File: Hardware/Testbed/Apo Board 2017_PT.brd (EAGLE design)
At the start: 96.5 x 62.2 mm, 18 parts

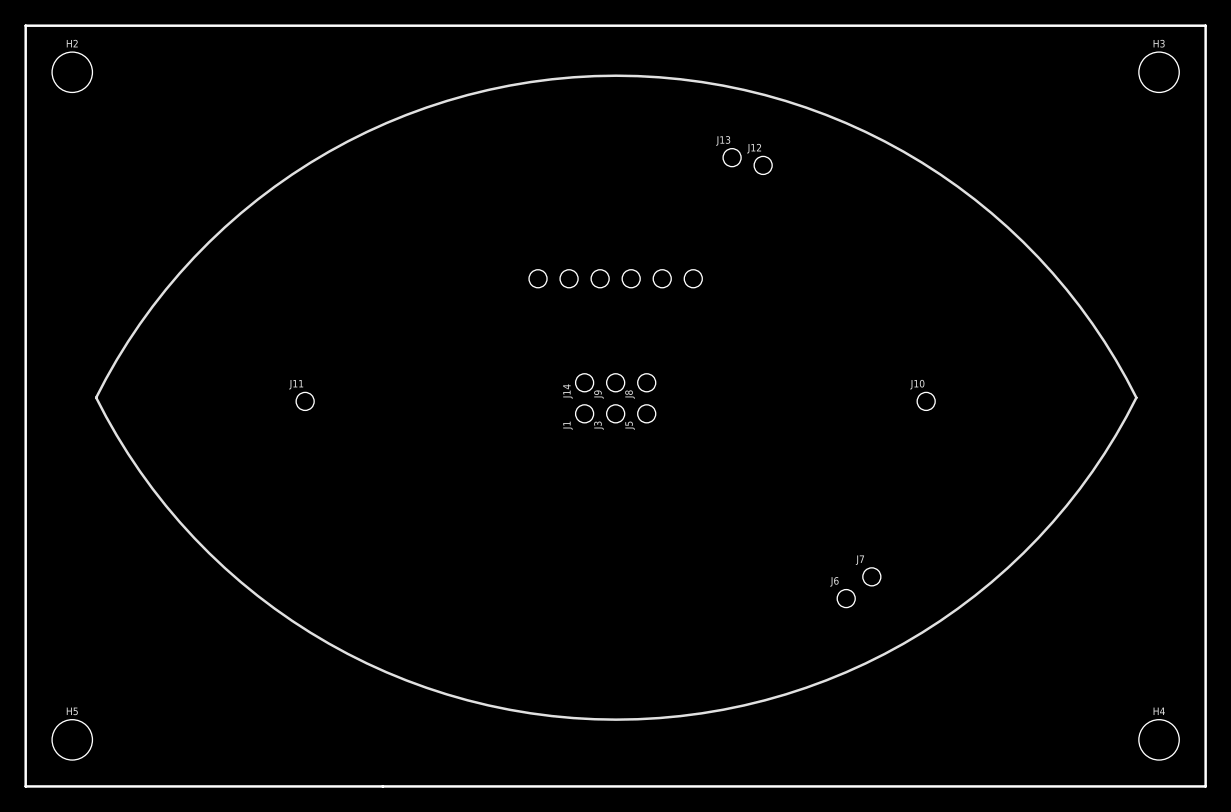
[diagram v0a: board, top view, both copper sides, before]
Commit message: Pogo Bed finished.
Finished making pogoed programming and testing fixture. Moving to
Hardware Folder
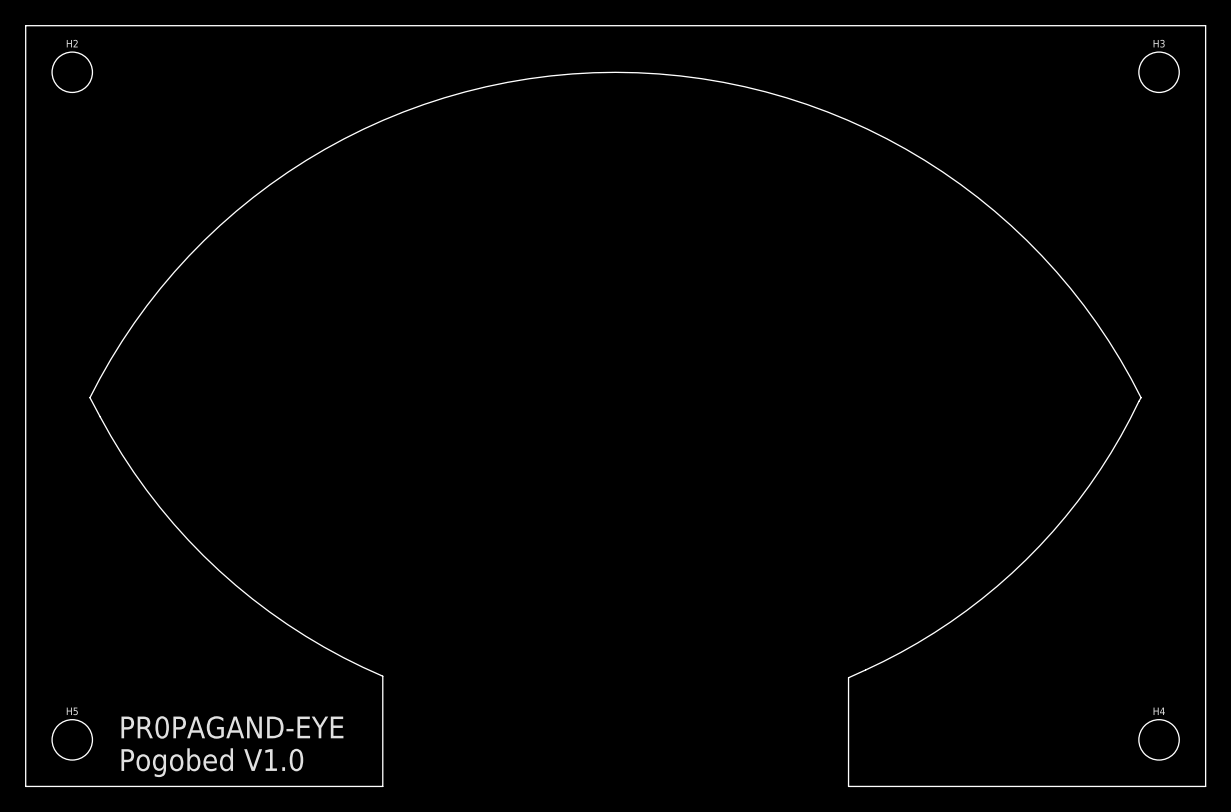
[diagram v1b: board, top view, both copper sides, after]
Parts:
- removed J1, J10, J11, J12, J13, J14, J3, J5, J6, J7, J8, J9: (no value), SparkFun-Connectors:1X01_POGOPIN_HOLE_0.58_DIA
- removed J4: (no value), SparkFun-Connectors:1X06_HOLES_ONLY
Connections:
- removed net N$13: J6.1, J7.1
- removed net N$15: J12.1
- removed net N$17: J13.1
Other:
- outline, holes or cut-outs redrawn
- board text added: "PR0PAGAND-EYE Pogobed V1.0"
- board text removed: "5V"
- board text removed: "A4"
- board text removed: "A5"
- board text removed: "DTR"
- board text removed: "GND"
- board text removed: "MISO"
- board text removed: "MOSI"
- board text removed: "RST"
- board text removed: "RX"
- board text removed: "SCK"
- board text removed: "SCL"
- board text removed: "SDA"
- board text removed: "TX"
